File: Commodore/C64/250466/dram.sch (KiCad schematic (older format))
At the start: 16 parts, among them U10 4464, U13 74LS257, U14 74LS258, U25 74LS257, U26 74LS373, U9 4464

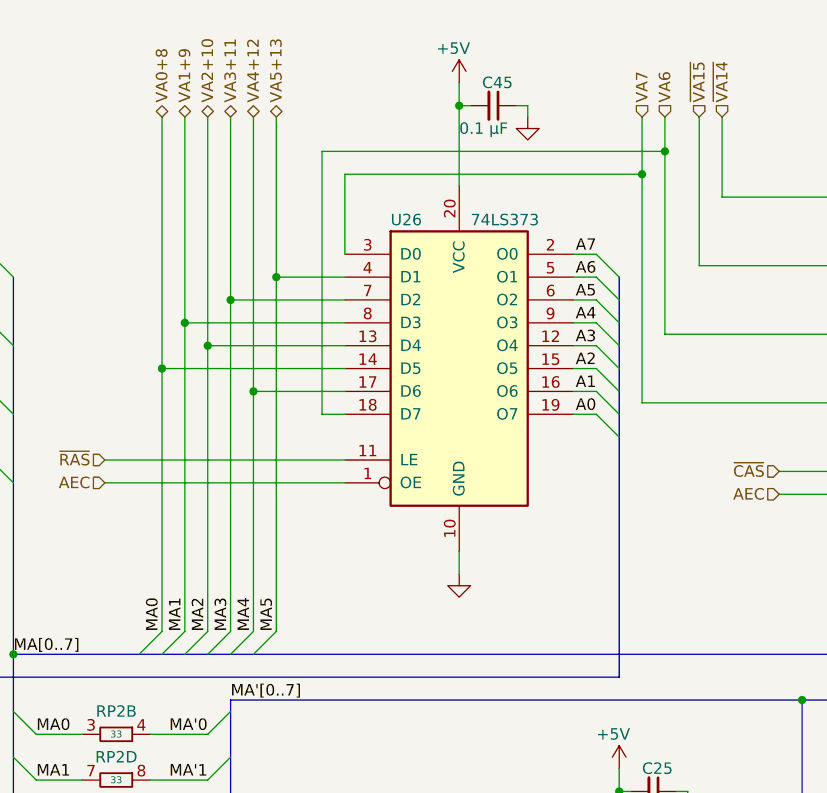
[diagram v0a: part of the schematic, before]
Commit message: Correct U26 pin usage on C64 #260466
The pin layout of 250466 for U26 seems to have changed from
251469. Correct the pin layout to match the board.
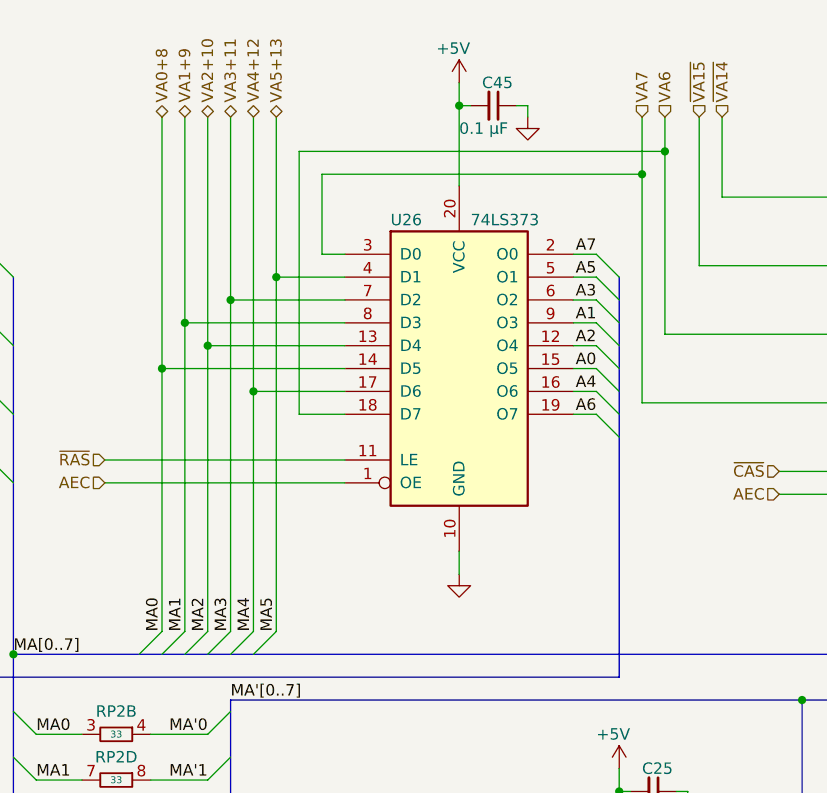
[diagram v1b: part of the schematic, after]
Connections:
- net A0: now also U26.15 (O5); no longer U26.19 (O7)
- net A1: now also U26.9 (O3); no longer U26.16 (O6)
- net A2: now also U26.12 (O4); no longer U26.15 (O5)
- net A3: now also U26.6 (O2); no longer U26.12 (O4)
- net A4: now also U26.16 (O6); no longer U26.9 (O3)
- net A5: now also U26.5 (O1); no longer U26.6 (O2)
- net A6: now also U26.19 (O7); no longer U26.5 (O1)
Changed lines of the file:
@@
 	3550 3250 3650 3150
-Wire Wire Line
-	3150 3150 3150 2000
-Wire Wire Line
-	3250 900  3250 1800
-Wire Wire Line
-	3350 900  3350 1900
-Wire Wire Line
-	3450 900  3450 1700
-Wire Wire Line
-	3550 900  3550 2100
 Wire Wire Line
 	6300 2150 5250 2150
@@
 	0    1    1    0
 $EndComp
-Wire Wire Line
-	3950 2000 3150 2000
-Connection ~ 3150 2000
-Wire Wire Line
-	3150 2000 3150 900
-Wire Wire Line
-	3250 1800 3950 1800
-Connection ~ 3250 1800
-Wire Wire Line
-	3250 1800 3250 3150
-Wire Wire Line
-	3350 1900 3950 1900
-Connection ~ 3350 1900
-Wire Wire Line
-	3350 1900 3350 3150
-Wire Wire Line
-	3450 1700 3950 1700
-Connection ~ 3450 1700
-Wire Wire Line
-	3450 1700 3450 3150
-Wire Wire Line
-	3550 2100 3950 2100
-Connection ~ 3550 2100
-Wire Wire Line
-	3550 2100 3550 3150
-Wire Wire Line
-	3950 1600 3650 1600
-Wire Wire Line
-	3650 900  3650 1600
-Connection ~ 3650 1600
-Wire Wire Line
-	3650 1600 3650 3150
-Wire Wire Line
-	5250 1150 3950 1150
-Wire Wire Line
-	3950 1150 3950 1500
 Connection ~ 5250 1150
 Wire Wire Line
 	5250 1150 5250 900
-Wire Wire Line
-	3950 2200 3850 2200
-Wire Wire Line
-	3850 2200 3850 1050
-Wire Wire Line
-	3850 1050 5350 1050
 Connection ~ 5350 1050
 Wire Wire Line
@@
 Text Label 5050 1500 2    50   ~ 0
 A7
+Text Label 5050 2200 2    50   ~ 0
+A6
 Text Label 5050 1600 2    50   ~ 0
-A6
+A5
+Text Label 5050 2100 2    50   ~ 0
+A4
 Text Label 5050 1700 2    50   ~ 0
-A5
+A3
+Text Label 5050 1900 2    50   ~ 0
+A2
 Text Label 5050 1800 2    50   ~ 0
-A4
-Text Label 5050 1900 2    50   ~ 0
-A3
+A1
 Text Label 5050 2000 2    50   ~ 0
-A2
-Text Label 5050 2100 2    50   ~ 0
-A1
-Text Label 5050 2200 2    50   ~ 0
 A0
 Text Label 3450 3450 0    50   ~ 0
@@
 Wire Wire Line
 	4550 6250 6650 6250
+Wire Wire Line
+	3550 900  3550 2100
+Wire Wire Line
+	3150 900  3150 2000
+Wire Wire Line
+	3350 900  3350 1900
+Wire Wire Line
+	3250 900  3250 1800
+Wire Wire Line
+	3450 900  3450 1700
+Wire Wire Line
+	3650 900  3650 1600
+Wire Wire Line
+	3950 2000 3150 2000
+Connection ~ 3150 2000
+Wire Wire Line
+	3150 2000 3150 3150
+Wire Wire Line
+	3950 1800 3250 1800
+Connection ~ 3250 1800
+Wire Wire Line
+	3250 1800 3250 3150
+Wire Wire Line
+	3950 1900 3350 1900
+Connection ~ 3350 1900
+Wire Wire Line
+	3350 1900 3350 3150
+Wire Wire Line
+	3950 1700 3450 1700
+Connection ~ 3450 1700
+Wire Wire Line
+	3450 1700 3450 3150
+Wire Wire Line
+	3950 2100 3550 2100
+Connection ~ 3550 2100
+Wire Wire Line
+	3550 2100 3550 3150
+Wire Wire Line
+	3950 1600 3650 1600
+Connection ~ 3650 1600
+Wire Wire Line
+	3650 1600 3650 3150
+Wire Wire Line
+	3950 1500 3850 1500
+Wire Wire Line
+	3850 1500 3850 1150
+Wire Wire Line
+	3850 1150 5250 1150
+Wire Wire Line
+	3750 1050 3750 2200
+Wire Wire Line
+	3750 2200 3950 2200
+Wire Wire Line
+	3750 1050 5350 1050
 Wire Bus Line
 	7550 1350 7550 3250
